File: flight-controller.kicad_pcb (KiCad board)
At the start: 2 copper layers, 35 x 45 mm, 16 parts, among them J1 USB_C_Receptacle, SW1 SW_Push, U1 ESP32-C3-WROOM-02, U2 MPU-6050, U3 AMS1117-3.3

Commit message: NEW - Implemented Ground plane on B.Cu to join all GNDs together. FIX - Rotated LDO to reduce length of 5v and 3.3v connection FIX - Moved C1 to reduce length of 5v connection NEW - All GNDs connected and wired up
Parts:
- moved C1 15.9 mm to (194.0, 66.5), turned to 90 degrees
- moved R1 1.25 mm to (202.0, 66.6)
- turned U3 to 90 degrees
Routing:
- net +5V: track 68.1 -> 37.0 mm, vias 2 -> 1
- net GND: track 0.00 -> 11.3 mm, vias 0 -> 14
- net +3.3V: track 67.1 -> 63.7 mm, vias 2 -> 0
- added copper zone on B.Cu, net GND

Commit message: Modified some routing to resolve some clearance issues
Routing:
- net +5V: track 37.0 -> 44.6 mm
- net GND: track 11.3 -> 10.9 mm, vias 14 -> 13
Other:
- board size 35 x 45 mm -> 35 x 51.5 mm
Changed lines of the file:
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@@
 	)
 	(gr_rect
-		(start 175.5 35)
+		(start 175.5 28.5)
 		(end 210.5 80)
 		(stroke
@@
 	)
 	(segment
+		(start 203.2 70.653284)
+		(end 203.2 69.825)
+		(width 0.2)
+		(layer "F.Cu")
+		(net "+5V")
+	)
+	(segment
+		(start 198.3 69.825)
+		(end 198.3 70.38241)
+		(width 0.2)
+		(layer "F.Cu")
+		(net "+5V")
+	)
+	(segment
 		(start 203.37 68.53)
 		(end 203.37 63.585)
@@
 	)
 	(segment
+		(start 198.3 70.38241)
+		(end 200.01759 72.1)
+		(width 0.2)
+		(layer "F.Cu")
+		(net "+5V")
+	)
+	(segment
 		(start 180.46 70.5)
 		(end 180.46 65.5)
@@
 	)
 	(segment
+		(start 200.01759 72.1)
+		(end 201.753284 72.1)
+		(width 0.2)
+		(layer "F.Cu")
+		(net "+5V")
+	)
+	(segment
 		(start 190.4 68.5)
 		(end 188.4 70.5)
@@
 	)
 	(segment
+		(start 201.753284 72.1)
+		(end 203.2 70.653284)
+		(width 0.2)
+		(layer "F.Cu")
+		(net "+5V")
+	)
+	(segment
 		(start 182.46 72.5)
 		(end 180.46 70.5)
@@
 	)
 	(segment
-		(start 198.77 57.285)
-		(end 198.77 56.985)
-		(width 0.2)
-		(layer "F.Cu")
-		(net "GND")
-	)
-	(segment
 		(start 199.97 53.585)
 		(end 199.97 52.53)
@@
 	)
 	(via
-		(at 198.77 57.285)
-		(size 0.6)
-		(drill 0.3)
-		(layers "F.Cu" "B.Cu")
-		(net "GND")
-	)
-	(via
 		(at 194 65)
 		(size 0.6)
@@
 		(drill 0.3)
 		(layers "F.Cu" "B.Cu")
-		(net "GND")
-	)
-	(segment
-		(start 198.715 57.285)
-		(end 198.77 57.285)
-		(width 0.2)
-		(layer "B.Cu")
 		(net "GND")
 	)
@@
 	)
 	(segment
+		(start 183 50)
+		(end 182.9 50.1)
+		(width 0.5)
+		(layer "F.Cu")
+		(net "+3.3V")
+	)
+	(segment
 		(start 178.3 51.15741)
 		(end 178.3 50.7)
@@
 	)
 	(segment
+		(start 182.9 50.1)
+		(end 181 50.1)
+		(width 0.5)
+		(layer "F.Cu")
+		(net "+3.3V")
+	)
+	(segment
 		(start 183.4 50)
 		(end 183.4 51.1)
@@
 	)
 	(segment
+		(start 183.4 50)
+		(end 183 50)
+		(width 0.5)
+		(layer "F.Cu")
+		(net "+3.3V")
+	)
+	(segment
 		(start 184.9 48.5)
 		(end 184.9 46.4)
@@
 	)
 	(segment
-		(start 183.4 50)
-		(end 181 50)
-		(width 0.5)
-		(layer "F.Cu")
-		(net "+3.3V")
-	)
-	(segment
 		(start 189.1 45.6)
 		(end 185.478119 45.6)
@@
 	)
 	(segment
-		(start 190.5 45)
-		(end 185.1 45)
-		(width 0.2)
-		(layer "F.Cu")
-		(net "/SDA")
-	)
-	(segment
 		(start 178.5 45)
 		(end 177.8 46.34259)
@@
 	)
 	(segment
+		(start 179.5 44.5)
+		(end 178.5 45)
+		(width 0.2)
+		(layer "F.Cu")
+		(net "/SDA")
+	)
+	(segment
+		(start 185.623918 45)
+		(end 185.49128 44.867362)
+		(width 0.2)
+		(layer "F.Cu")
+		(net "/SDA")
+	)
+	(segment
+		(start 190.5 45)
+		(end 185.623918 45)
+		(width 0.2)
+		(layer "F.Cu")
+		(net "/SDA")
+	)
+	(segment
 		(start 183.9 45)
-		(end 178.5 45)
+		(end 179.5 44.5)
 		(width 0.2)
 		(layer "F.Cu")
@@
 	)
 	(via
-		(at 185.1 45)
+		(at 185.49128 44.867362)
 		(size 0.6)
 		(drill 0.3)
@@
 	)
 	(segment
-		(start 185.1 45)
+		(start 185.358642 45)
 		(end 183.9 45)
 		(width 0.2)
 		(layer "B.Cu")
+		(net "/SDA")
+	)
+	(segment
+		(start 185.49128 44.867362)
+		(end 185.358642 45)
+		(width 0.2)
+		(layer "B.Cu")

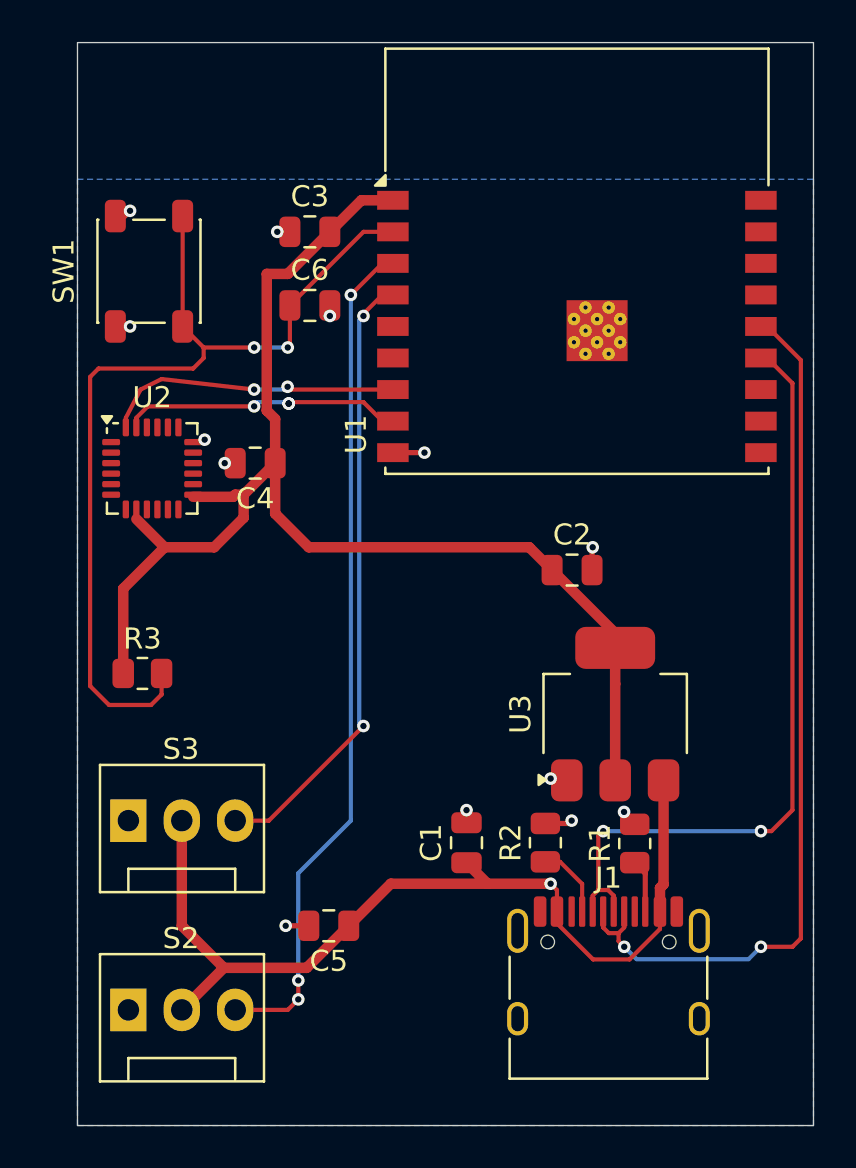
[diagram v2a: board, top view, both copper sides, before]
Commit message: - Redid all the traces from scratch with a much clearer design plan - Much cleaner paths, large and thick powerlines, thinner and more direct signal lines Ground plate works better now
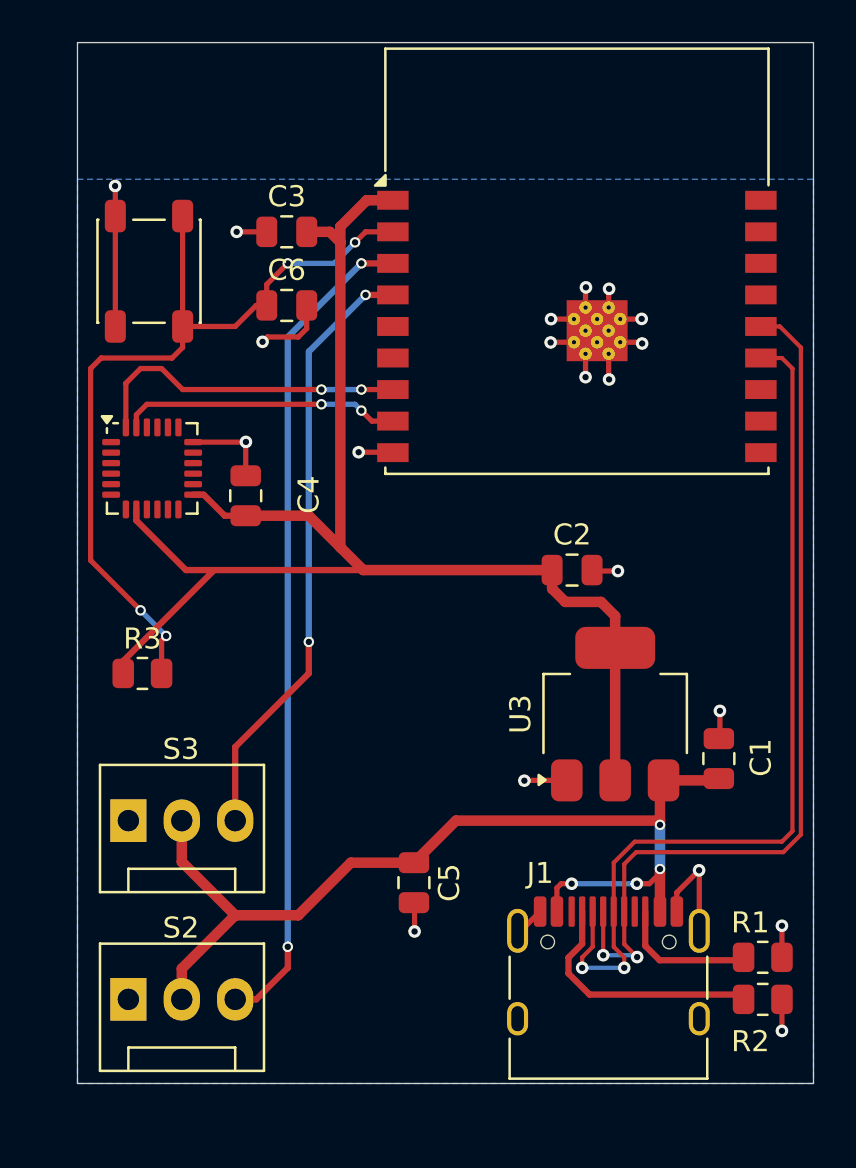
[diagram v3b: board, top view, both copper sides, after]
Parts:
- J1: value USB_C_Receptacle -> USB_C_Receptacle_USB2.0_16P
- moved R2 12.7 mm to (208.1, 74.0), turned to 0 degrees
- moved C1 12.6 mm to (206.0, 62.5)
- moved R1 8.15 mm to (208.1, 72.0), turned to 0 degrees
- moved C5 4.54 mm to (191.5, 68.5), turned to -90 degrees
- moved C4 1.61 mm to (183.5, 50.0), turned to 90 degrees
- moved C3 1.10 mm to (185.4, 37.5)
- moved C6 1.10 mm to (185.4, 41.0)
- moved S2 0.50 mm to (177.9, 74.0)
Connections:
- J1 pad A1: unconnected-(J1-GND-PadA1) -> GND
- J1 pad A12: unconnected-(J1-GND-PadA1)_3 -> GND
- J1 pad B1: unconnected-(J1-GND-PadA1)_2 -> GND
- J1 pad B12: unconnected-(J1-GND-PadA1)_1 -> GND
- J1 pad SH: unconnected-(J1-SHIELD-PadSH) -> GND
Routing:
- net GND: track 10.9 -> 41.6 mm, vias 13 -> 20
- net Net-(J1-CC1): track 3.50 -> 12.0 mm
- net +3.3V: track 63.7 -> 69.9 mm
- net /USB_D-: track 37.3 -> 42.9 mm
- net Net-(U1-EN): track 45.0 -> 39.6 mm, vias 2 -> 4
- net Net-(J1-CC2): track 2.53 -> 6.65 mm
- net +5V: track 44.6 -> 48.0 mm, vias 1 -> 4
- net /SDA: track 14.2 -> 15.5 mm
- net /SERVO1: track 40.4 -> 39.6 mm, vias 3 -> 2
- net /SERVO2: track 29.7 -> 29.1 mm
- net /SCL: track 13.6 -> 13.3 mm, vias 3 -> 2
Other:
- board size 35 x 51.5 mm -> 35 x 49.5 mm

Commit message: Adjusted version silkscreen
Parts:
- moved C2 3.03 mm to (202.1, 53.6)
- renumbered S2 to SERVO1, S3 to SERVO2
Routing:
- net +3.3V: track 69.9 -> 70.7 mm
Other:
- board size 35 x 49.5 mm -> 35 x 43 mm
- board text added: "C Labs TVC Rev 0.1 062026"
- board text added: "ESP32"
- board text added: "GND 5V SIG"
- board text added: "MPU-6050"
- board text added: "RST"
- board text added: "USB-C"
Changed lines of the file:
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@@
 			(at -3.25 -5.87 0)
 			(layer "F.SilkS")
+			(hide yes)
 			(effects
 				(font
@@
 		(descr "3-pin CPU fan Through hole pin header, see http://www.formfactors.org/developer%5Cspecs%5Crev1_2_public.pdf")
 		(tags "pin header 3-pin CPU fan")
-		(property "Reference" "S2"
-			(at 2.5 -3.4 0)
+		(property "Reference" "SERVO1"
+			(at 7.58 0.5 90)
 			(layer "F.SilkS")
 			(effects
@@
 		(descr "3-pin CPU fan Through hole pin header, see http://www.formfactors.org/developer%5Cspecs%5Crev1_2_public.pdf")
 		(tags "pin header 3-pin CPU fan")
-		(property "Reference" "S3"
-			(at 2.5 -3.4 0)
+		(property "Reference" "SERVO2"
+			(at 7.58 0.5 90)
 			(layer "F.SilkS")
 			(effects
@@
 			(at 0.05 2 90)
 			(layer "F.SilkS")
+			(hide yes)
 			(effects
 				(font
@@
 			(at 0 -1.68 90)
 			(layer "F.SilkS")
+			(hide yes)
 			(effects
 				(font
@@
 	(footprint "Capacitor_SMD:C_0805_2012Metric"
 		(layer "F.Cu")
-		(at 199.02 53.585)
+		(at 202.05 53.58)
 		(descr "Capacitor SMD 0805 (2012 Metric), square (rectangular) end terminal, IPC-7351 nominal, (Body size source: IPC-SM-782 page 76, https://www.pcb-3d.com/wordpress/wp-content/uploads/ipc-sm-782a_amendment_1_and_2.pdf, https://docs.google.com/spreadsheets/d/1BsfQQcO9C6DZCsRaXUlFlo91Tg2WpOkGARC1WS5S8t0/edit?usp=sharing)")
 		(tags "capacitor")
@@
 			(at 0 -1.68 0)
 			(layer "F.SilkS")
+			(hide yes)
 			(effects
 				(font
@@
 			(at -0.5875 -1.65 0)
 			(layer "F.SilkS")
+			(hide yes)
 			(effects
 				(font
@@
 			(at 0 -4.5 90)
 			(layer "F.SilkS")
+			(hide yes)
 			(effects
 				(font
@@
 			(at -0.5875 2 0)
 			(layer "F.SilkS")
+			(hide yes)
 			(effects
 				(font
@@
 			(at 0 -1.68 0)
 			(layer "F.SilkS")
+			(hide yes)
 			(effects
 				(font
@@
 			(at 0.05 3 90)
 			(layer "F.SilkS")
+			(hide yes)
 			(effects
 				(font
@@
 			(at 0 -1.68 0)
 			(layer "F.SilkS")
+			(hide yes)
 			(effects
 				(font
@@
 	)
 	(gr_rect
-		(start 175.5 28.5)
+		(start 175.5 35)
 		(end 210.5 78)
 		(stroke
@@
 		(layer "Edge.Cuts")
 	)
+	(gr_text "MPU-6050\n"
+		(at 180 52.5 0)
+		(layer "F.SilkS")
+		(effects
+			(font
+				(size 1 1)
+				(thickness 0.15)
+			)
+		)
+	)
+	(gr_text "GND 5V SIG\n"
+		(at 180.5 62 0)
+		(layer "F.SilkS")
+		(effects
+			(font
+				(size 1 1)
+				(thickness 0.15)
+			)
+		)
+	)
+	(gr_text "GND 5V SIG\n"
+		(at 180.5 70 0)
+		(layer "F.SilkS")
+		(effects
+			(font
+				(size 1 1)
+				(thickness 0.15)
+			)
+		)
+	)
+	(gr_text "C Labs\nTVC Rev 0.1\n062026"
+		(at 192.28 56.25 0)
+		(layer "F.SilkS")
+		(effects
+			(font
+				(size 1 1)
+				(thickness 0.15)
+			)
+		)
+	)
+	(gr_text "ESP32"
+		(at 199 50 0)
+		(layer "F.SilkS")
+		(effects
+			(font
+				(size 1 1)
+				(thickness 0.15)
+			)
+		)
+	)
+	(gr_text "USB-C\n"
+		(at 200.5 67.5 0)
+		(layer "F.SilkS")
+		(effects
+			(font
+				(size 1 1)
+				(thickness 0.15)
+			)
+		)
+	)
+	(gr_text "RST"
+		(at 182.5 39.5 90)
+		(layer "F.SilkS")
+		(effects
+			(font
+				(size 1 1)
+				(thickness 0.15)
+			)
+		)
+	)
 	(segment
 		(start 191.53 70.77)
@@
 	)
 	(segment
+		(start 203 53.58)
+		(end 204.31 53.58)
+		(width 0.25)
+		(layer "F.Cu")
+		(net "GND")
+	)
+	(segment
 		(start 184.5 37.5)
 		(end 183.07 37.5)
@@
 	)
 	(segment
-		(start 201.2 53.63)
-		(end 200.015 53.63)
-		(width 0.25)
-		(layer "F.Cu")
-		(net "GND")
-	)
-	(segment
 		(start 199.11 42.75)
 		(end 198.01 42.75)
@@
 	)
 	(segment
+		(start 204.31 53.58)
+		(end 204.36 53.63)
+		(width 0.25)
+		(layer "F.Cu")
+		(net "GND")
+	)
+	(segment
 		(start 201.31 42.75)
 		(end 202.29 42.75)
@@
 	)
 	(segment
-		(start 200.015 53.63)
-		(end 199.97 53.585)
-		(width 0.25)
-		(layer "F.Cu")
-		(net "GND")
-	)
-	(segment
 		(start 184.53 42.5)
 		(end 184.3 42.73)
@@
 	)
 	(via
-		(at 201.2 53.63)
+		(at 183.07 37.5)
 		(size 0.6)
 		(drill 0.3)
@@
 	)
 	(via
-		(at 183.07 37.5)
+		(at 204.36 53.63)
 		(size 0.6)
 		(drill 0.3)
@@
 	)
 	(segment
+		(start 201.07 57.285)
+		(end 201.07 53.61)
+		(width 0.5)
+		(layer "F.Cu")
+		(net "+3.3V")
+	)
+	(segment
 		(start 189.25 36)
 		(end 190.5 36)
@@
 	)
 	(segment
-		(start 198.7 55.1)
-		(end 198.07 54.47)
+		(start 189.085 53.585)
+		(end 188 52.5)
 		(width 0.5)
 		(layer "F.Cu")
@@
 	)
 	(segment
-		(start 189.085 53.585)
-		(end 188 52.5)
+		(start 201.07 63.585)
+		(end 201.07 57.285)
 		(width 0.5)
 		(layer "F.Cu")
@@
 	)
 	(segment
-		(start 201.07 63.585)
-		(end 201.07 57.285)
+		(start 198.07 53.585)
+		(end 198.075 53.58)
 		(width 0.5)
 		(layer "F.Cu")
@@
 	)
 	(segment
-		(start 201.07 57.285)
-		(end 201.07 55.77)
-		(width 0.5)
-		(layer "F.Cu")
-		(net "+3.3V")
-	)
-	(segment
-		(start 198.07 54.47)
-		(end 198.07 53.585)
-		(width 0.5)
-		(layer "F.Cu")
-		(net "+3.3V")
-	)
-	(segment
 		(start 187.5 37.5)
 		(end 188 38)
@@
 	)
 	(segment
-		(start 200.4 55.1)
-		(end 198.7 55.1)
-		(width 0.5)
-		(layer "F.Cu")
-		(net "+3.3V")
-	)
-	(segment
 		(start 182.5 51)
 		(end 183.5 51)
@@
 	)
 	(segment
+		(start 198.075 53.58)
+		(end 201.1 53.58)
+		(width 0.5)
+		(layer "F.Cu")
+		(net "+3.3V")
+	)
+	(segment
 		(start 178.3 51.22812)
 		(end 180.65688 53.585)
@@
 	)
 	(segment
-		(start 201.07 55.77)
-		(end 200.4 55.1)
+		(start 201.07 53.61)
+		(end 201.1 53.58)
 		(width 0.5)
 		(layer "F.Cu")
